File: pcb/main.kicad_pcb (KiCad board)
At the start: 4 copper layers, 165.1 x 50.8 mm, 49 parts, among them Q1 BC337, U1 LM358, U2 LM358, U3 LM358, U4 LM358, U5 LM358, U6 LM358

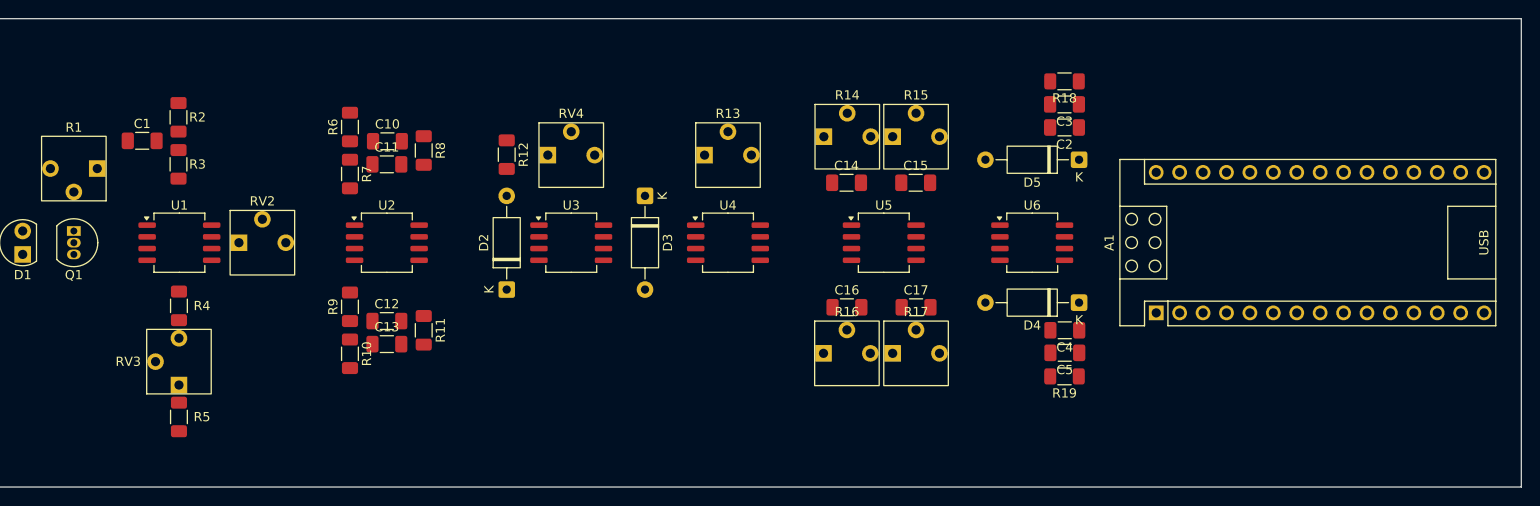
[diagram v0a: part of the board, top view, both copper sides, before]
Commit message: Placed the touchpoints and power stuff.
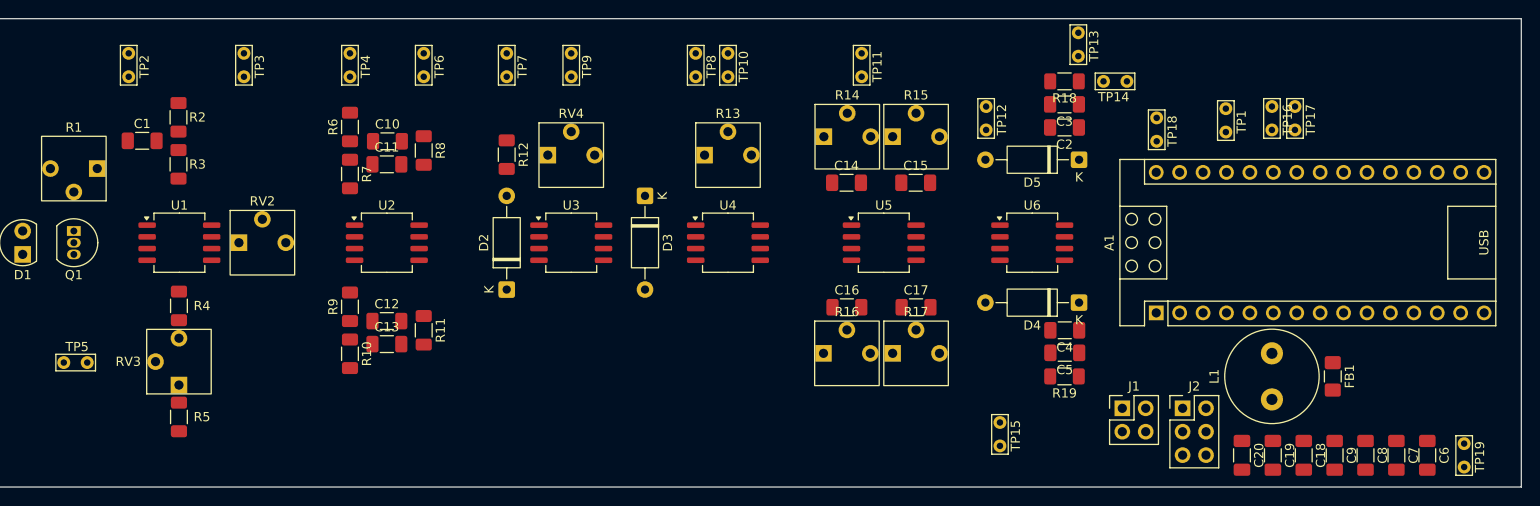
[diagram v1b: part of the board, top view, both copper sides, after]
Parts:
- added C18: 47n, Capacitor_SMD:C_1206_3216Metric_Pad1.33x1.80mm_HandSolder, F.Cu at (205.5, 121.6)
- added C19: 10n, Capacitor_SMD:C_1206_3216Metric_Pad1.33x1.80mm_HandSolder, F.Cu at (202.1, 121.6)
- added C20: 1n, Capacitor_SMD:C_1206_3216Metric_Pad1.33x1.80mm_HandSolder, F.Cu at (198.8, 121.6)
- added C6: 1u, Capacitor_SMD:C_1206_3216Metric_Pad1.33x1.80mm_HandSolder, F.Cu at (218.9, 121.6)
- added C7: 220n, Capacitor_SMD:C_1206_3216Metric_Pad1.33x1.80mm_HandSolder, F.Cu at (215.5, 121.6)
- added C8: 470n, Capacitor_SMD:C_1206_3216Metric_Pad1.33x1.80mm_HandSolder, F.Cu at (212.2, 121.6)
- added C9: 100n, Capacitor_SMD:C_1206_3216Metric_Pad1.33x1.80mm_HandSolder, F.Cu at (208.8, 121.6)
- added FB1: 100R @ 100MHz, Inductor_SMD:L_1206_3216Metric_Pad1.42x1.75mm_HandSolder, F.Cu at (208.6, 113.0)
- added J1: Conn_02x02_Row_Letter_First, Connector_PinHeader_2.54mm:PinHeader_2x02_P2.54mm_Vertical, F.Cu at (185.8, 116.5)
- added J2: Conn_02x03_Row_Letter_First, Connector_PinHeader_2.54mm:PinHeader_2x03_P2.54mm_Vertical, F.Cu at (192.3, 116.5)
- added L1: 20m, Inductor_THT:L_Radial_D10.0mm_P5.00mm_Neosid_SD12k_style3, F.Cu at (202.0, 115.5)
- added TP1: TestPoint, TestPoint:TestPoint_Bridge_Pitch2.54mm_Drill0.7mm, F.Cu at (197.0, 86.5)
- added TP10: TestPoint, TestPoint:TestPoint_Bridge_Pitch2.54mm_Drill0.7mm, F.Cu at (143.0, 80.5)
- added TP11: TestPoint, TestPoint:TestPoint_Bridge_Pitch2.54mm_Drill0.7mm, F.Cu at (157.5, 80.5)
- added TP12: TestPoint, TestPoint:TestPoint_Bridge_Pitch2.54mm_Drill0.7mm, F.Cu at (171.0, 86.3)
- added TP13: TestPoint, TestPoint:TestPoint_Bridge_Pitch2.54mm_Drill0.7mm, F.Cu at (181.0, 78.3)
- added TP14: TestPoint, TestPoint:TestPoint_Bridge_Pitch2.54mm_Drill0.7mm, F.Cu at (183.7, 81.0)
- added TP15: TestPoint, TestPoint:TestPoint_Bridge_Pitch2.54mm_Drill0.7mm, F.Cu at (172.5, 120.5)
- added TP16: TestPoint, TestPoint:TestPoint_Bridge_Pitch2.54mm_Drill0.7mm, F.Cu at (202.0, 86.3)
- added TP17: TestPoint, TestPoint:TestPoint_Bridge_Pitch2.54mm_Drill0.7mm, F.Cu at (204.5, 86.3)
- added TP18: TestPoint, TestPoint:TestPoint_Bridge_Pitch2.54mm_Drill0.7mm, F.Cu at (189.5, 87.5)
- added TP19: TestPoint, TestPoint:TestPoint_Bridge_Pitch2.54mm_Drill0.7mm, F.Cu at (222.9, 122.8)
- added TP2: TestPoint, TestPoint:TestPoint_Bridge_Pitch2.54mm_Drill0.7mm, F.Cu at (78.0, 80.5)
- added TP3: TestPoint, TestPoint:TestPoint_Bridge_Pitch2.54mm_Drill0.7mm, F.Cu at (90.5, 80.5)
- added TP4: TestPoint, TestPoint:TestPoint_Bridge_Pitch2.54mm_Drill0.7mm, F.Cu at (102.0, 80.5)
- added TP5: TestPoint, TestPoint:TestPoint_Bridge_Pitch2.54mm_Drill0.7mm, F.Cu at (73.5, 111.5)
- added TP6: TestPoint, TestPoint:TestPoint_Bridge_Pitch2.54mm_Drill0.7mm, F.Cu at (110.0, 80.5)
- added TP7: TestPoint, TestPoint:TestPoint_Bridge_Pitch2.54mm_Drill0.7mm, F.Cu at (119.0, 80.5)
- added TP8: TestPoint, TestPoint:TestPoint_Bridge_Pitch2.54mm_Drill0.7mm, F.Cu at (139.5, 80.5)
- added TP9: TestPoint, TestPoint:TestPoint_Bridge_Pitch2.54mm_Drill0.7mm, F.Cu at (126.0, 80.5)
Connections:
- A1 pad 30: unconnected-(A1-VIN-Pad30) -> Net-(A1-VIN)
- A1 pad 5: unconnected-(A1-D2-Pad5) -> Net-(A1-D2)
- A1 pad 6: unconnected-(A1-D3-Pad6) -> Net-(A1-D3)
- A1 pad 7: unconnected-(A1-D4-Pad7) -> Net-(A1-D4)
- D1 pad 1: +5V -> +5VA
- R1 pad 1: +5V -> +5VA
- R2 pad 1: +5V -> +5VA
- R4 pad 1: +5V -> +5VA
- U1 pad 8: +5V -> +5VA
- U2 pad 8: +5V -> +5VA
- U3 pad 8: +5V -> +5VA
- U4 pad 8: +5V -> +5VA
- U5 pad 8: +5V -> +5VA
- U6 pad 1: signal -> Net-(A1-D2)

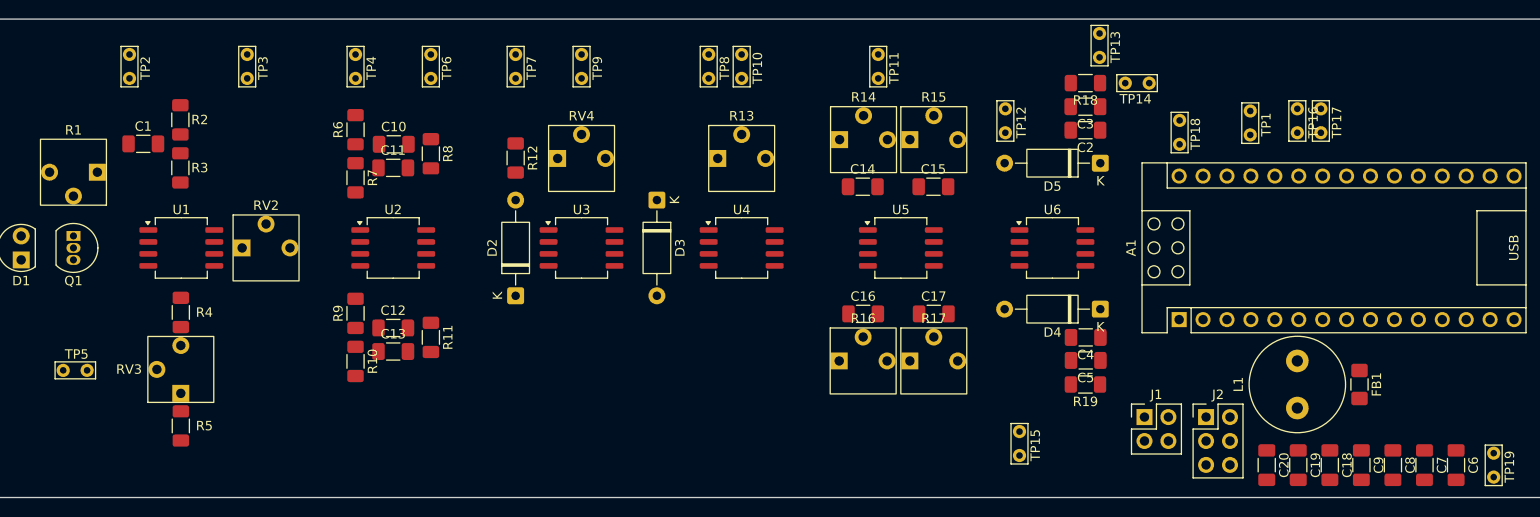
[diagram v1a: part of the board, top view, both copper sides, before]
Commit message: Adjusted potentiometer values and reannotated.
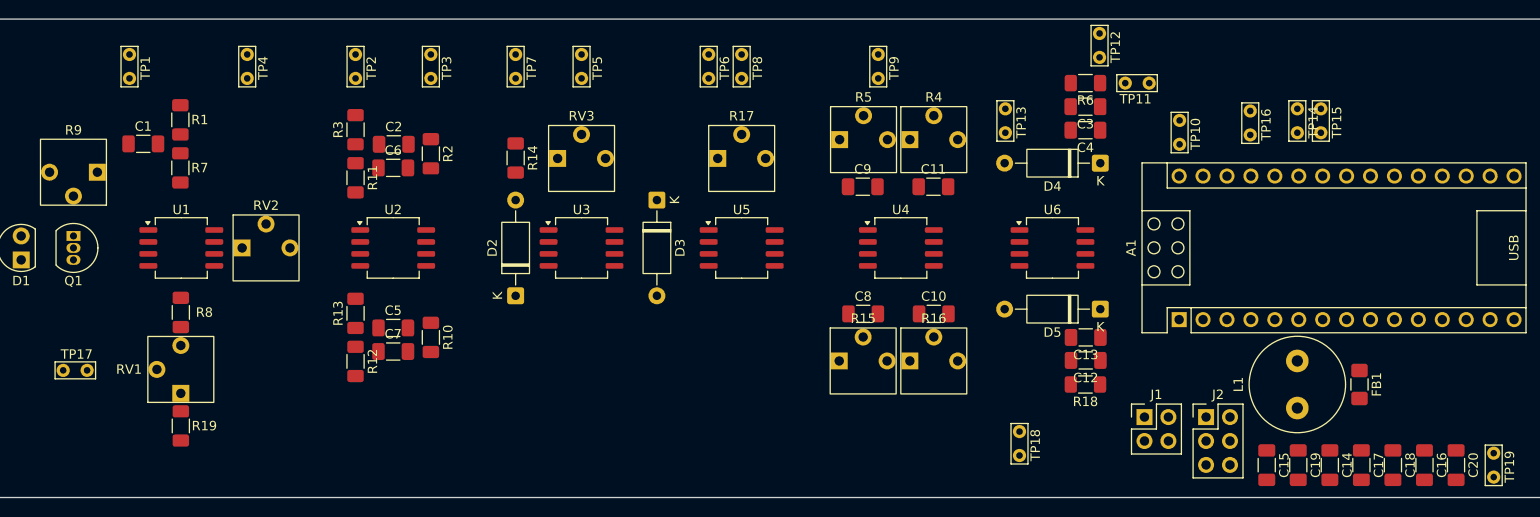
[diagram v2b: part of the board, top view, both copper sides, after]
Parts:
- R15: renamed from R16; value 100k -> 20k
- R16: renamed from R17; value 100k -> 20k
- R17: renamed from R13; value 100k -> 20k
- R4: renamed from R15; value 100k -> 20k
- R5: renamed from R14; value 100k -> 20k
- RV1: renamed from RV3; value 100k -> 1k
- renumbered C17 to C10, C15 to C11, C5 to C12, C4 to C13, C18 to C14, C20 to C15, C7 to C16, C9 to C17, C8 to C18, C10 to C2, C6 to C20, C2 to C4, C12 to C5, C11 to C6, C13 to C7, C16 to C8, C14 to C9, D5 to D4, D4 to D5, R2 to R1, R11 to R10, R7 to R11, R10 to R12, R9 to R13, R12 to R14, R19 to R18, R5 to R19, R8 to R2, R6 to R3, R18 to R6, R3 to R7, R4 to R8, R1 to R9, RV4 to RV3, TP2 to TP1, TP18 to TP10, TP14 to TP11, TP13 to TP12, TP12 to TP13, TP16 to TP14, TP17 to TP15, TP1 to TP16, TP5 to TP17, TP15 to TP18, TP4 to TP2, TP6 to TP3, TP3 to TP4, TP9 to TP5, TP8 to TP6, TP10 to TP8, TP11 to TP9, U5 to U4, U4 to U5

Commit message: Routed things out.
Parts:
- moved TP14 1.26 mm to (201.8, 87.5)
- moved TP15 1.23 mm to (204.5, 87.5)
- moved TP16 1.00 mm to (197.1, 87.5)
- moved C2 0.75 mm to (106.0, 86.8)
- moved C5 0.75 mm to (106.0, 106.2)
- moved D1 0.50 mm to (67.0, 98.5)
- moved C14 0.38 mm to (205.5, 121.9)
- moved C15 0.38 mm to (198.8, 121.9)
- moved C16 0.38 mm to (215.5, 121.9)
- moved C17 0.38 mm to (208.8, 121.9)
- moved C18 0.38 mm to (212.2, 121.9)
- moved C19 0.38 mm to (202.1, 121.9)
- moved C20 0.38 mm to (218.9, 121.9)
- moved TP10 0.25 mm to (189.4, 87.2)
- moved C6 0.25 mm to (106.0, 90.2)
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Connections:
- RV3 pad 1: +5V -> +5VA
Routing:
- net Net-(A1-D2): track 0.00 -> 60.1 mm
- net Net-(U5A--): track 0.00 -> 56.1 mm
- net +5V: track 0.00 -> 51.8 mm, vias 0 -> 1
- net Net-(U1B-+): track 0.00 -> 51.1 mm, vias 0 -> 3
- net Net-(D4-K): track 0.00 -> 47.8 mm, vias 0 -> 1
- net Net-(R3-Pad2): track 0.00 -> 45.2 mm
- net Net-(D5-K): track 0.00 -> 42.9 mm, vias 0 -> 1
- net Net-(C5-Pad2): track 0.00 -> 42.7 mm
- net Net-(D5-A): track 0.00 -> 42.4 mm, vias 0 -> 1
- net Net-(U3B-+): track 0.00 -> 37.5 mm
- net Net-(C2-Pad2): track 0.00 -> 35.6 mm
- net Net-(U1A--): track 0.00 -> 33.1 mm
- net Net-(D2-A): track 0.00 -> 32.1 mm, vias 0 -> 3
- net Net-(D4-A): track 0.00 -> 28.2 mm
- net Net-(Q1-C): track 0.00 -> 25.1 mm
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- added copper zone on B.Cu, net +5VA
- added copper zone on F.Cu, net +5VA
